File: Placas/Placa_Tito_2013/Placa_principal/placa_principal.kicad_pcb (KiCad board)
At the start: 2 copper layers, 65 x 104 mm, 91 parts, among them IC1 ATMEGA88A-A, K1 Servo, P1 ADICIONAL 5V, P10 Batería 3,6V, P2 ADICIONAL GND, P3 ADICIONAL 5V, P4 ADICIONAL GND, P5 Puerto Serie, P6 Programador, P7 Motor 1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

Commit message: Seguimos posicionando componentes en el PBC
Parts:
- C10, C11, C15, C2, C3, C5, R11, R12, R14, R16, R7, R8: moved to B.Cu
- moved JP3 131.8 mm to (52.1, 142.2), turned to 270 degrees
- moved R11 130.0 mm to (50.8, 73.7), turned to 270 degrees
- moved JP2 128.8 mm to (55.9, 142.2), turned to 270 degrees
- moved JP1 124.9 mm to (64.8, 115.6), turned to 270 degrees
- moved C3 120.5 mm to (49.5, 95.2)
- moved R7 115.8 mm to (38.1, 106.7), turned to 270 degrees
- moved R12 115.5 mm to (53.3, 73.7), turned to 270 degrees
- moved R16 115.0 mm to (74.9, 73.7), turned to 270 degrees
- moved R14 114.4 mm to (69.8, 73.7), turned to 270 degrees
- moved C2 112.6 mm to (49.5, 100.3)
- moved Q1 107.7 mm to (59.7, 86.4), turned to 90 degrees
- moved C11 103.3 mm to (71.1, 80.0), turned to 180 degrees
- moved C9 99.1 mm to (54.6, 55.9)
- moved X1 97.4 mm to (49.5, 95.2), turned to 90 degrees
- moved C10 90.2 mm to (72.4, 92.7), turned to 180 degrees
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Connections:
- C11 pad 1: (no net) -> N-0000037

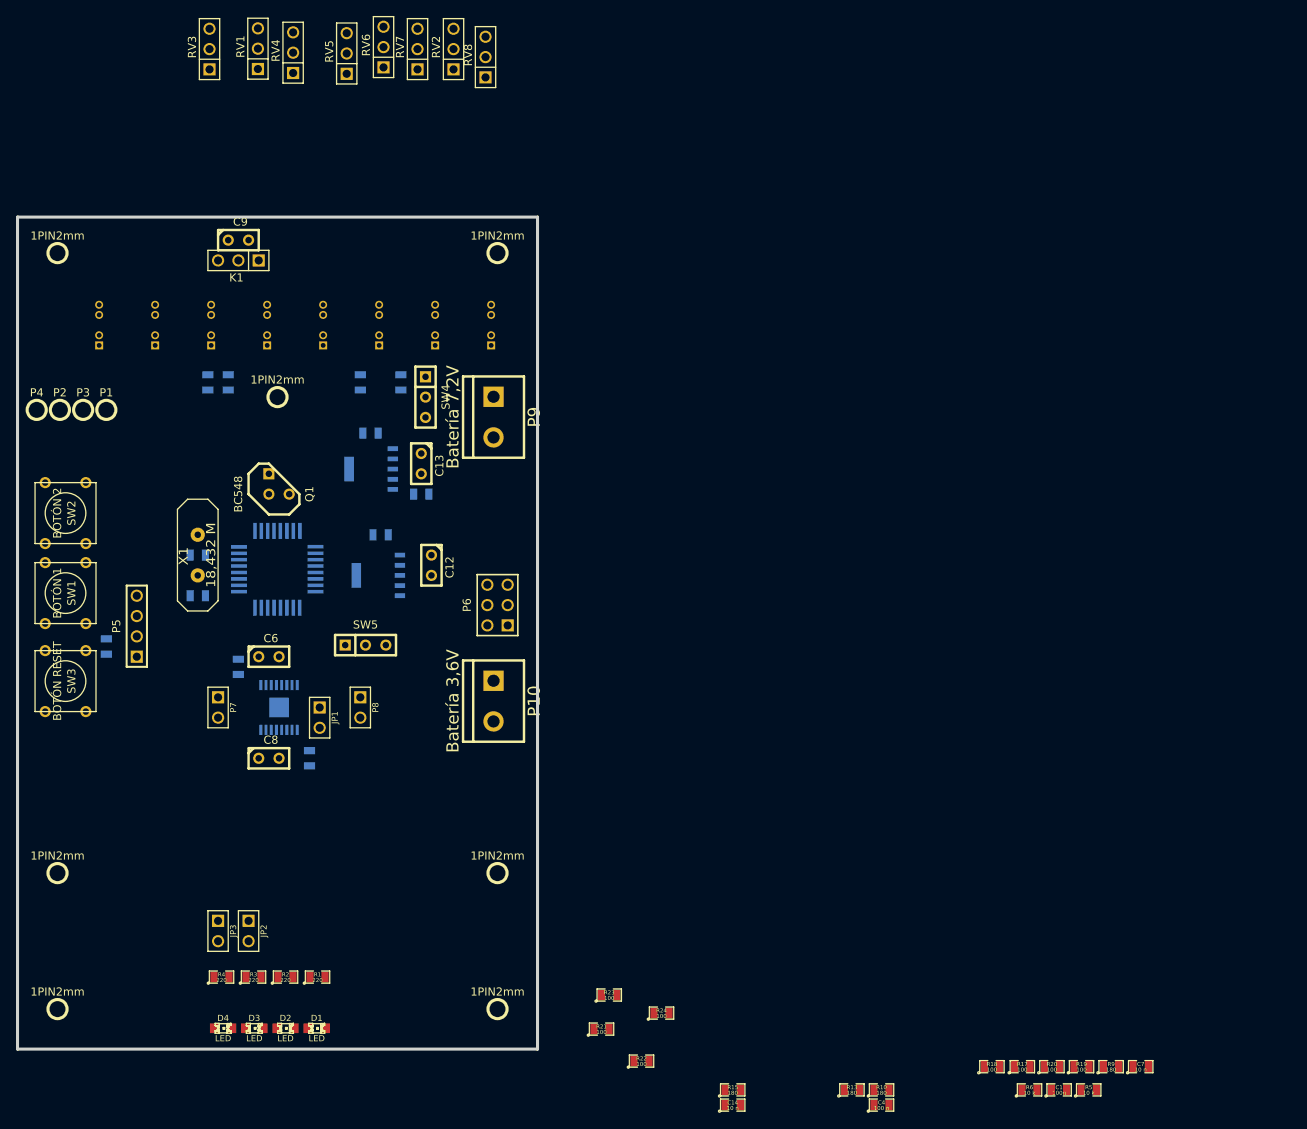
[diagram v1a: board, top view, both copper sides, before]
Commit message: Terminamos de posicionar componentes, y comenzamos el routeo
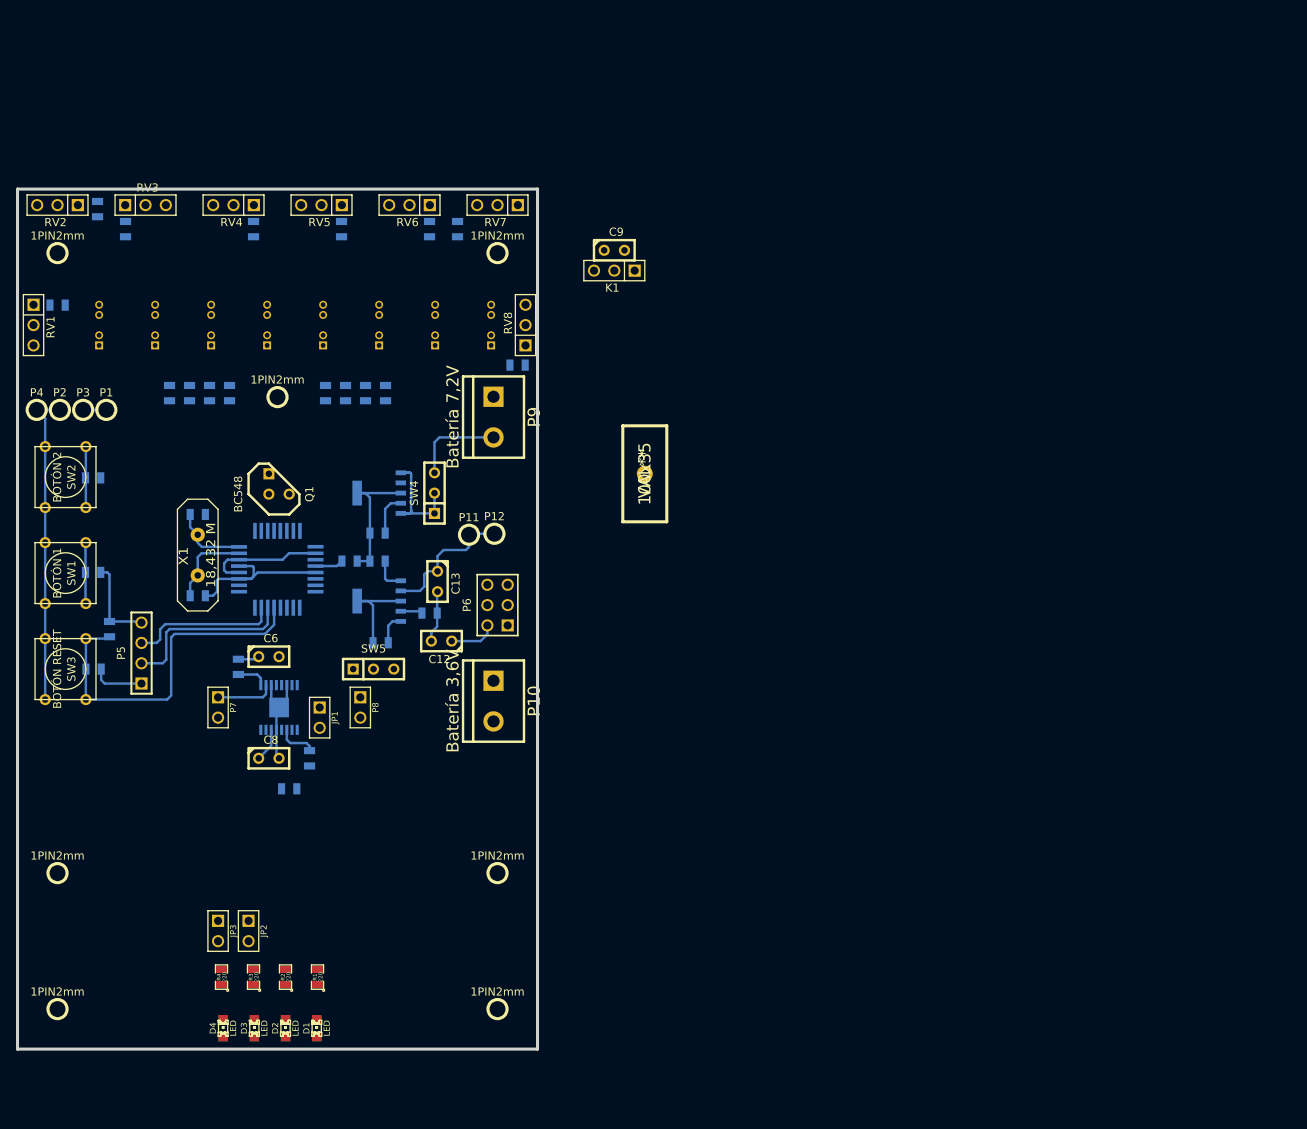
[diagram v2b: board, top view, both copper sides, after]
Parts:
- added 100x35: VAL**, 100x35, F.Cu at (105.4, 85.1)
- added P11: ADICIONAL 3,3V, 1PIN2mm, F.Cu at (83.4, 92.7)
- added P12: ADICIONAL 3,3V, 1PIN2mm, F.Cu at (86.6, 92.6)
- C1, C14, C4, C7, R10, R13, R15, R17, R18, R19, R20, R21, R22, R23, R24, R5, R6, R9: moved to B.Cu
- moved R19 158.9 mm to (40.5, 54.5), turned to 270 degrees
- moved R18 154.9 mm to (37.0, 52.0), turned to 270 degrees
- moved R17 153.6 mm to (32.0, 64.0)
- moved R9 144.7 mm to (46.0, 75.0), turned to 270 degrees
- moved R20 144.6 mm to (56.5, 54.5), turned to 270 degrees
- moved R5 140.3 mm to (36.4, 97.4), turned to 180 degrees
- moved R6 139.8 mm to (36.4, 85.6), turned to 180 degrees
- moved R10 122.8 mm to (48.5, 75.0), turned to 270 degrees
- moved C4 112.6 mm to (36.5, 109.5)
- moved C7 112.0 mm to (61.0, 124.5), turned to 180 degrees
- moved C1 110.6 mm to (68.5, 96.0)
- moved R13 109.2 mm to (65.5, 75.0), turned to 270 degrees
- moved R22 107.3 mm to (78.5, 54.5), turned to 270 degrees
- moved R21 105.1 mm to (67.5, 54.5), turned to 270 degrees
- moved R15 98.5 mm to (70.5, 75.0), turned to 270 degrees
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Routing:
- net GND: track 0.00 -> 115.6 mm
- net /RESET: track 0.00 -> 44.5 mm
- net +5V: track 0.00 -> 34.7 mm
- net /RX: track 0.00 -> 21.9 mm
- net N-0000038: track 0.00 -> 19.8 mm
- net /TX: track 0.00 -> 18.6 mm
- net +3.3V: track 0.00 -> 17.6 mm
- net VDD: track 0.00 -> 11.4 mm
- net /Xtal1: track 0.00 -> 10.6 mm
- net /Xtal2: track 0.00 -> 9.31 mm
- net /BOTÓN 2: track 0.00 -> 7.66 mm
- net /BOTÓN 1: track 0.00 -> 7.66 mm
- net /Control Motores/MOTOR A SALIDA 1: track 0.00 -> 7.29 mm
- net N-0000039: track 0.00 -> 5.27 mm
- net N-0000047: track 0.00 -> 4.96 mm
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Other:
- board size 65 x 104 mm -> 65 x 107.5 mm
- net class Default: trace_width 0.508 -> 0.3048

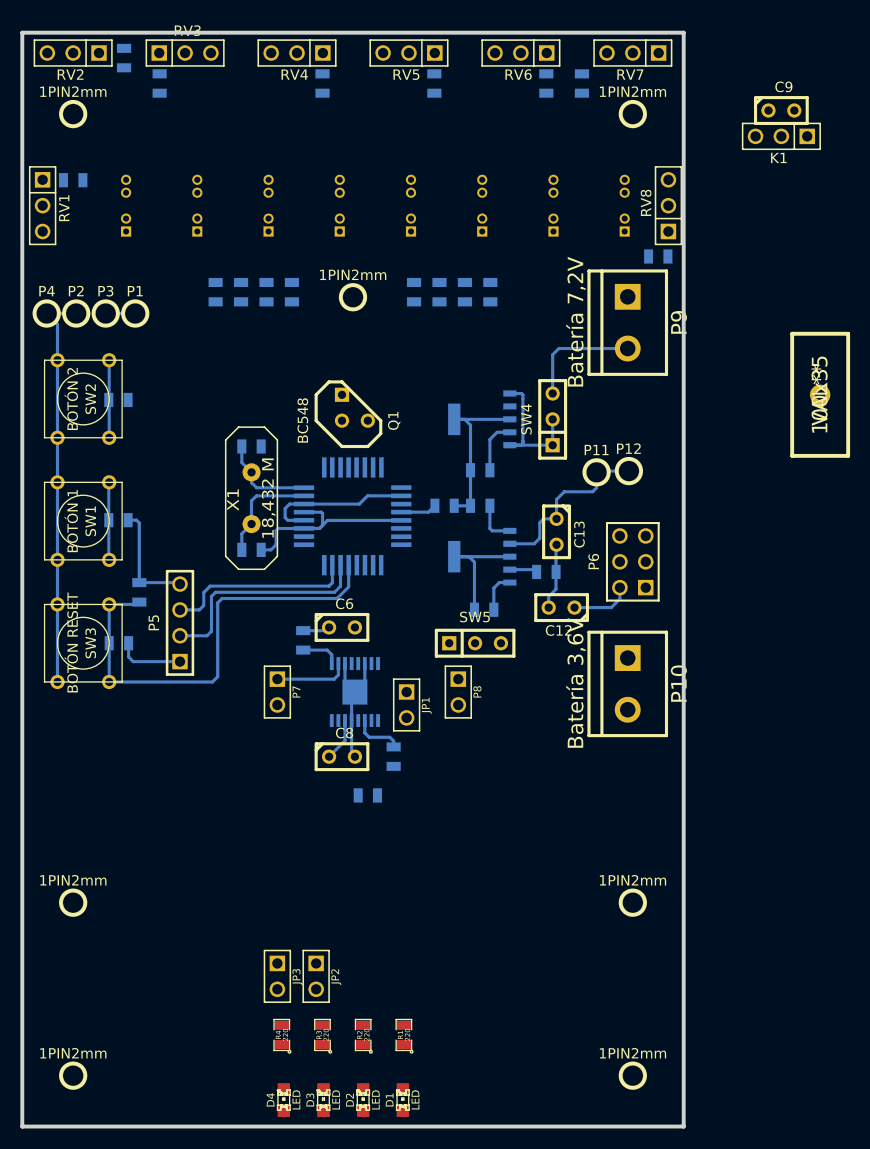
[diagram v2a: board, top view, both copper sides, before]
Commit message: Ruteada placa.
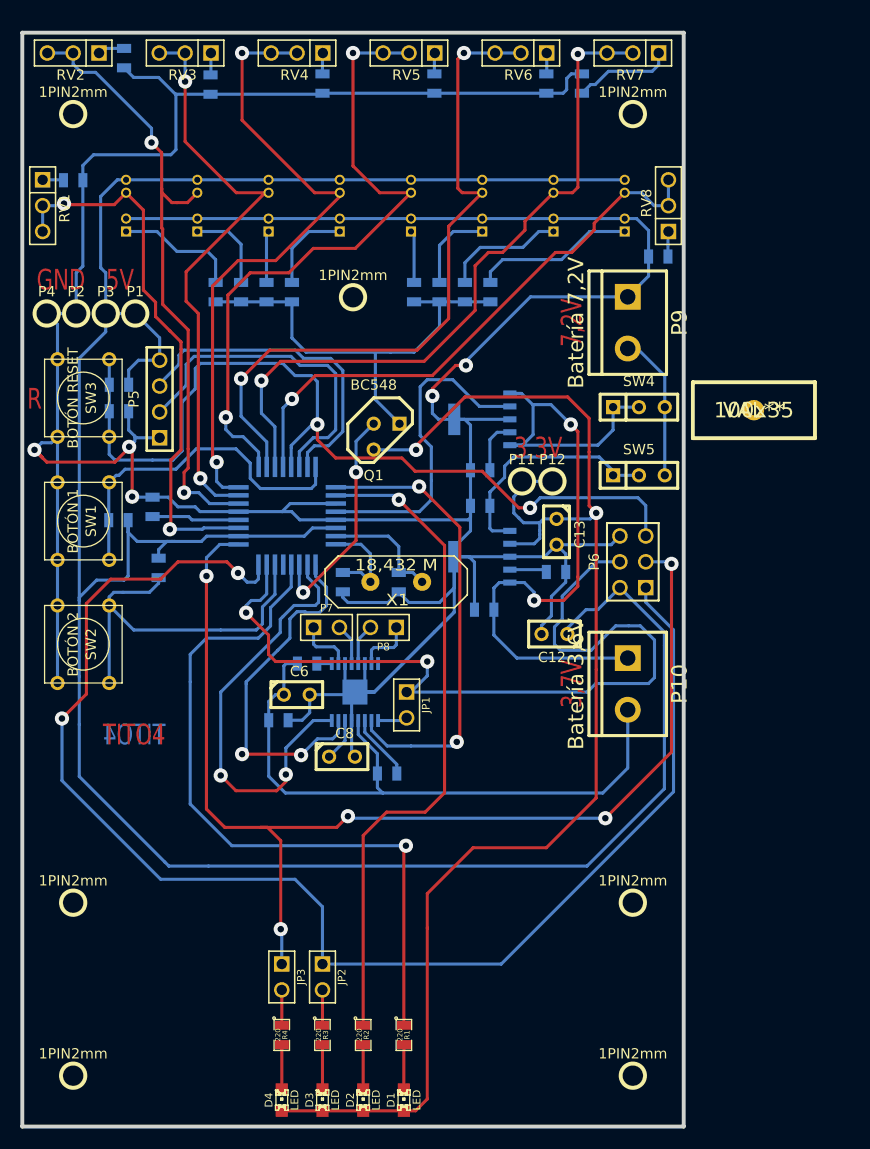
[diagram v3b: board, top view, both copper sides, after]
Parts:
- removed C9: 100 u, C1
- removed K1: Servo, PIN_ARRAY_3X1
- moved C1 28.7 mm to (39.8, 96.1), turned to 90 degrees
- moved SW2 24.1 mm to (33.0, 109.6)
- moved SW3 24.1 mm to (33.0, 85.4)
- moved SW5 23.1 mm to (87.6, 93.0)
- moved C4 22.8 mm to (36.5, 86.7)
- moved P5 22.1 mm to (40.5, 85.5)
- moved R7 20.5 mm to (36.5, 84.1), turned to 180 degrees
- moved R6 17.0 mm to (40.4, 102.1), turned to 270 degrees
- moved X1 16.4 mm to (63.8, 103.5), turned to 180 degrees
- moved C3 16.1 mm to (58.5, 103.5), turned to 270 degrees
- moved C2 14.8 mm to (64.0, 103.5), turned to 270 degrees
- moved C7 11.5 mm to (52.2, 117.1), turned to 0 degrees
- moved P8 9.73 mm to (62.5, 108.0), turned to 180 degrees
- moved SW4 8.56 mm to (87.6, 86.3), turned to 0 degrees
- moved P7 7.98 mm to (56.9, 108.0), turned to 0 degrees
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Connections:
- IC1 pad 13: /Control Motores/Control Servo -> (no net)
- IC1 pad 19: /Sensores/Sensor 7 -> /Sensores/Sensor 1
- IC1 pad 22: /Sensores/Sensor 8 -> /Sensores/Sensor 2
- IC1 pad 23: /Sensores/Sensor 1 -> /Sensores/Sensor 3
- IC1 pad 24: /Sensores/Sensor 2 -> /Sensores/Sensor 4
- IC1 pad 25: /Sensores/Sensor 3 -> /Sensores/Sensor 5
- IC1 pad 26: /Sensores/Sensor 4 -> /Sensores/Sensor 6
- IC1 pad 27: /Sensores/Sensor 5 -> /Sensores/Sensor 7
- IC1 pad 28: /Sensores/Sensor 6 -> /Sensores/Sensor 8
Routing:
- net GND: track 115.6 -> 397.0 mm, vias 0 -> 5
- net +5V: track 34.7 -> 285.5 mm
- net /MISO: track 0.00 -> 138.4 mm, vias 0 -> 2
- net +3.3V: track 17.6 -> 137.5 mm, vias 0 -> 2
- net /SCK: track 0.00 -> 113.9 mm, vias 0 -> 5
- net /MOSI: track 0.00 -> 83.5 mm, vias 0 -> 2
- net /LED1: track 0.00 -> 71.3 mm, vias 0 -> 1
- net /Sensores/Sensor 7: track 0.00 -> 69.6 mm, vias 0 -> 2
- net /Sensores/Sensor 6: track 0.00 -> 68.0 mm, vias 0 -> 2
- net /LED2: track 0.00 -> 65.4 mm, vias 0 -> 1
- net /Sensores/Sensor 5: track 0.00 -> 64.4 mm, vias 0 -> 2
- net /Sensores/Sensor 4: track 0.00 -> 62.8 mm, vias 0 -> 2
- net /Sensores/Sensor 2: track 0.00 -> 61.9 mm, vias 0 -> 2
- net +BATT: track 2.67 -> 64.2 mm
- net /Sensores/Sensor 3: track 0.00 -> 58.3 mm, vias 0 -> 2
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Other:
- board text added: "3,3V"
- board text added: "3,7V"
- board text added: "5V"
- board text added: "7,2V"
- board text added: "GND"
- board text added: "R"
- board text added: "TITO4"

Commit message: Retoques a la placa, archivos de fabricación
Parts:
- removed 100x35: VAL**, 100x35
- moved R6 0.90 mm to (40.4, 103.0)
- moved P8 0.85 mm to (62.5, 108.8)
- moved P7 0.85 mm to (56.9, 108.8)
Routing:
- net GND: track 397.0 -> 442.6 mm
- net +5V: track 285.5 -> 319.9 mm
- net /PIN HABILITADOR: track 22.4 -> 41.7 mm
- net /MISO: track 138.4 -> 156.5 mm, vias 2 -> 3
- net /SCK: track 113.9 -> 129.4 mm, vias 5 -> 4
- net /MOSI: track 83.5 -> 68.5 mm, vias 2 -> 4
- net /RESET: track 88.7 -> 102.6 mm
- net +3.3V: track 137.5 -> 148.3 mm
- net +BATT: track 64.2 -> 74.3 mm
- net N-0000063: track 9.86 -> 19.7 mm
- net /Sensores/Sensor 2: track 61.9 -> 71.3 mm
- net N-0000039: track 76.0 -> 84.4 mm
- net /Sensores/Sensor 8: track 55.9 -> 63.8 mm
- net /Control Motores/Motor A Entrada 1: track 42.7 -> 49.6 mm
- net /Sensores/Sensor 4: track 62.8 -> 69.0 mm
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- added copper zone on B.Cu, net GND
- added copper zone on F.Cu, net GND
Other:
- net class Default: via_dia 1.397 -> 1.7; via_drill 0.635 -> 0.7
- rule trace_min: 0.2032 -> 0.3048
- board text added: "1"
- board text added: "2"
